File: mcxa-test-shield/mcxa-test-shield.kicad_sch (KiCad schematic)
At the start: 49 parts, among them J101 AIN0_short, J102 A7, J103 Digital/PWM, J104 Power, J105 IN0, J106 P2_2, J107 Analog, J108 Digital/PWM, J109 AIN1_short, J110 OUT0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

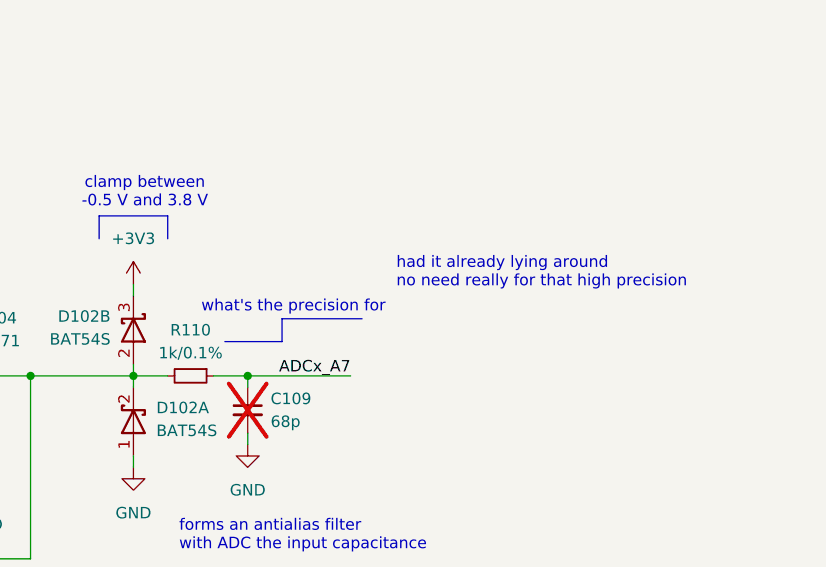
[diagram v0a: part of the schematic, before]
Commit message: add pdf schematic for the attenuator shield too
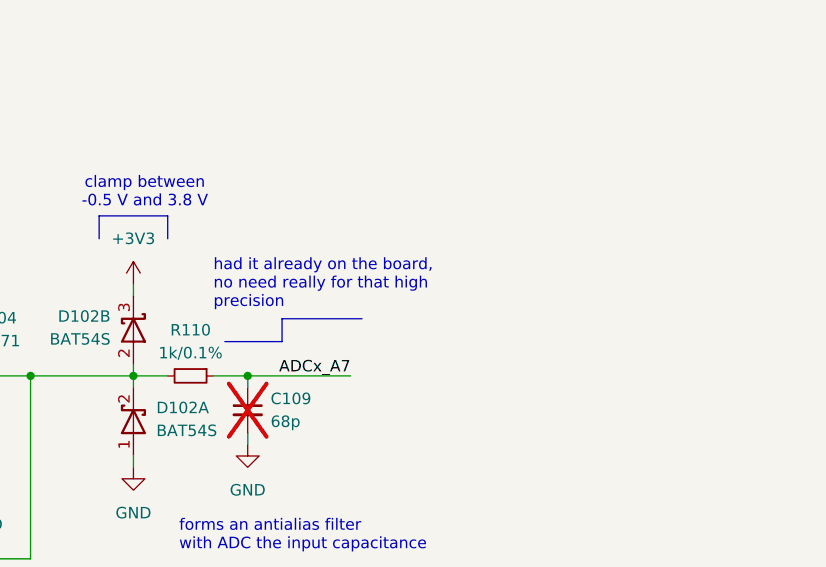
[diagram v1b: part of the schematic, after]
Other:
- note added: "had it already on the board, no need really for that high precision"
- note removed: "had it already lying around no need really for that high precision"
- note removed: "what's the precision for"
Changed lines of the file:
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@@
-		)
-	)
-	(text "what's the precision for"
-		(exclude_from_sim no)
-		(at 265.43 110.49 0)
-		(effects
-			(font
-				(size 1.27 1.27)
-			)
 		)
 	)
@@
 		)
 	)
-	(text "had it already lying around\nno need really for that high precision"
+	(text "had it already on the board,\nno need really for that high\nprecision"
 		(exclude_from_sim no)
-		(at 276.86 106.68 0)
+		(at 256.54 107.95 0)
 		(effects
 			(font
